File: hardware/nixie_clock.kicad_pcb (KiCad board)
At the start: 2 copper layers, 224 x 70 mm, 66 parts, among them J1 Conn_02x02_Odd_Even, J2 USB_C_Receptacle_USB2.0_16P, J3 Conn_01x04, Q1 IRF740, SW1 SW_SPST, SW2 SW_SPST, U1 AP63203WU, U2 MAX1771xSA, U3 ESP32-C3-WROOM-02, U4 HV5622PG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

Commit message: Change power connector.
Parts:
- J3: value Conn_01x04 -> Conn_01x03; footprint TerminalBlock_Phoenix:TerminalBlock_Phoenix_PT-1,5-4-3.5-H_1x04_P3.50mm_Horizontal -> TerminalBlock_Phoenix:TerminalBlock_Phoenix_PT-1,5-3-3.5-H_1x03_P3.50mm_Horizontal
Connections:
- J3 pad 3: /connectors/GND -> /connectors/12V
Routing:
- net /connectors/12V: track 326.0 -> 330.2 mm
- net /connectors/GND: track 118.5 -> 117.7 mm

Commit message: Rework some tracks.
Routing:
- net Net-(J1-Pin_3): track 11.7 -> 13.5 mm
- net /cpu/GPIO1: track 155.9 -> 157.5 mm
- net /cpu/GPIO2: track 154.1 -> 155.3 mm
- net /driver_3_digits_1_dot_left/SPI_SDO: track 147.0 -> 148.0 mm
- net /connectors/GND: track 117.7 -> 118.6 mm
- net Net-(J1-Pin_1): track 11.0 -> 11.8 mm

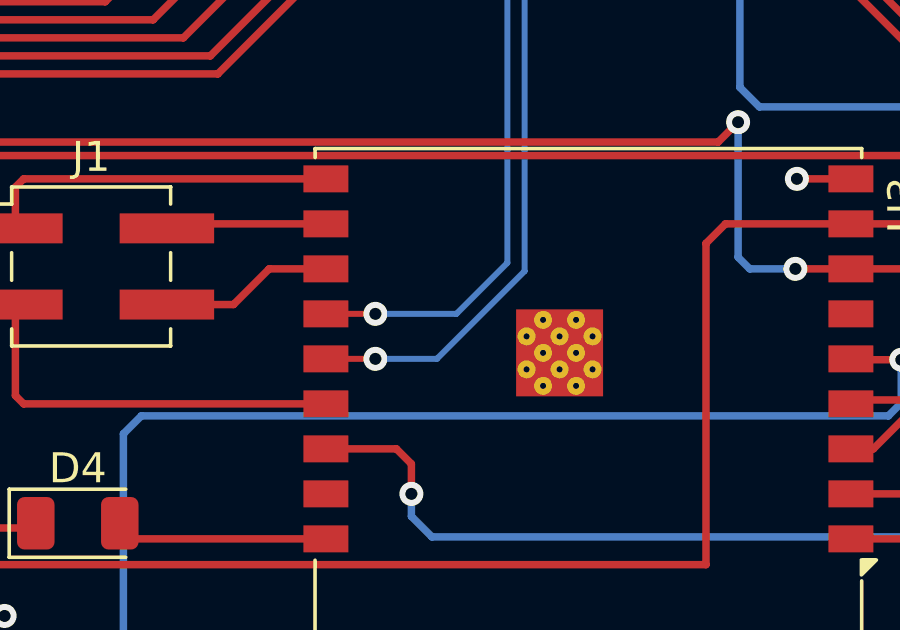
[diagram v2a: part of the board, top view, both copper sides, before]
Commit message: Fix USB lane size.
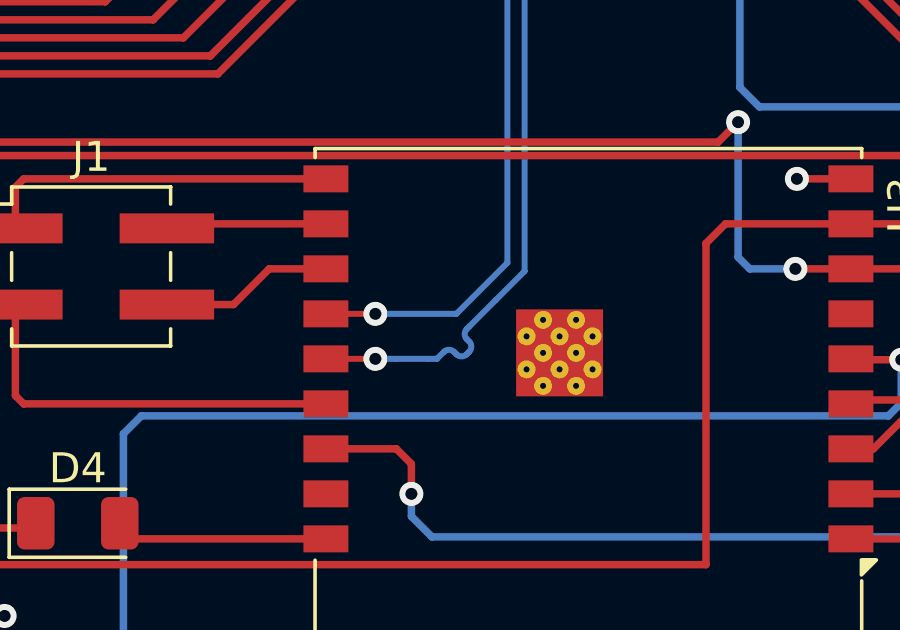
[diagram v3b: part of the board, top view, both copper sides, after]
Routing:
- net /connectors/D+: track 56.4 -> 57.1 mm
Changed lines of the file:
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@@
 	)
 	(segment
+		(start 157.641741 115.646581)
+		(end 157.726593 115.561728)
+		(width 0.2)
+		(layer "B.Cu")
+		(net 24)
+	)
+	(segment
 		(start 154.6 115.8)
+		(end 155.279866 115.8)
+		(width 0.2)
+		(layer "B.Cu")
+		(net 24)
+	)
+	(segment
+		(start 155.279866 115.8)
+		(end 156.351108 115.8)
+		(width 0.2)
+		(layer "B.Cu")
+		(net 24)
+	)
+	(segment
+		(start 156.65 115.8)
+		(end 156.883169 115.566831)
+		(width 0.2)
+		(layer "B.Cu")
+		(net 24)
+	)
+	(segment
+		(start 158.608049 113.841951)
+		(end 159.574 112.876)
+		(width 0.2)
+		(layer "B.Cu")
+		(net 24)
+	)
+	(segment
+		(start 159.574 73.601)
+		(end 161.075 72.1)
+		(width 0.2)
+		(layer "B.Cu")
+		(net 24)
+	)
+	(segment
+		(start 156.351108 115.8)
 		(end 156.65 115.8)
 		(width 0.2)
@@
 	)
 	(segment
+		(start 157.731697 114.718302)
+		(end 158.608049 113.841951)
+		(width 0.2)
+		(layer "B.Cu")
+		(net 24)
+	)
+	(segment
+		(start 157.646842 114.803154)
+		(end 157.731697 114.718302)
+		(width 0.2)
+		(layer "B.Cu")
+		(net 24)
+	)
+	(segment
+		(start 157.726593 115.222316)
+		(end 157.646842 115.142565)
+		(width 0.2)
+		(layer "B.Cu")
+		(net 24)
+	)
+	(segment
 		(start 161.075 72.1)
 		(end 162.505 72.1)
@@
 	)
 	(segment
-		(start 159.574 73.601)
-		(end 161.075 72.1)
+		(start 157.22258 115.566831)
+		(end 157.30233 115.646581)
 		(width 0.2)
 		(layer "B.Cu")
 		(net 24)
 	)
-	(segment
-		(start 156.65 115.8)
-		(end 159.574 112.876)
+	(arc
+		(start 156.883169 115.566831)
+		(mid 157.052874 115.496537)
+		(end 157.22258 115.566831)
+		(width 0.2)
+		(layer "B.Cu")
+		(net 24)
+	)
+	(arc
+		(start 157.30233 115.646581)
+		(mid 157.472036 115.716875)
+		(end 157.641741 115.646581)
+		(width 0.2)
+		(layer "B.Cu")
+		(net 24)
+	)
+	(arc
+		(start 157.726593 115.561728)
+		(mid 157.796888 115.392022)
+		(end 157.726593 115.222316)
+		(width 0.2)
+		(layer "B.Cu")
+		(net 24)
+	)
+	(arc
+		(start 157.646842 115.142565)
+		(mid 157.576547 114.97286)
+		(end 157.646842 114.803154)
 		(width 0.2)
 		(layer "B.Cu")
@@
 		)
 	)
+	(generated
+		(type tuning_pattern)
+		(name "Tuning Pattern")
+		(layer "B.Cu")
+		(base_line
+			(pts
+				(xy 155.279866 115.8) (xy 156.351108 115.8)
+			)
+		)
+		(corner_radius_percent 80)
+		(end
+			(xy 156.351108 115.8)
+		)
+		(initial_side "right")
+		(last_diff_pair_gap 0.18)
+		(last_netname "/connectors/D+")
+		(last_status "too_short")
+		(last_track_width 0.2)
+		(last_tuning "57,0357 mm (trop court)")
+		(max_amplitude 1)
+		(min_amplitude 0.2)
+		(min_spacing 0.6)
+		(origin
+			(xy 155.279866 115.8)
+		)
+		(override_custom_rules no)
+		(rounded yes)
+		(single_sided no)
+		(target_length 57.8092)
+		(target_length_max 57.9092)
+		(target_length_min 57.7092)
+		(target_skew 0)
+		(target_skew_max 0.1)
+		(target_skew_min -0.1)
+		(tuning_mode "single")
+		(members "35a16607-4558-4146-b2c9-206f343f8f7a")
+	)
+	(generated
+		(type tuning_pattern)
+		(name "Tuning Pattern")
+		(layer "B.Cu")
+		(base_line
+			(pts
+				(xy 156.883169 115.566831) (xy 158.608049 113.841951)
+			)
+		)
+		(corner_radius_percent 80)
+		(end
+			(xy 158.608049 113.841951)
+		)
+		(initial_side "right")
+		(last_diff_pair_gap 0.18)
+		(last_netname "/connectors/D+")
+		(last_status "tuned")
+		(last_track_width 0.2)
+		(last_tuning "57,8092 mm (ajusté)")
+		(max_amplitude 1)
+		(min_amplitude 0.2)
+		(min_spacing 0.6)
+		(origin
+			(xy 156.883169 115.566831)
+		)
+		(override_custom_rules no)
+		(rounded yes)
+		(single_sided no)
+		(target_length 57.8092)
+		(target_length_max 57.9092)
+		(target_length_min 57.7092)
+		(target_skew 0)
+		(target_skew_max 0.1)
+		(target_skew_min -0.1)
+		(tuning_mode "single")
+		(members "10d51b2e-0cfd-4ea9-9fbd-f867cd2565ff" "2f0039b8-3d12-499b-b6d5-722cef66da14"
+			"43471335-dcd3-473c-9966-2fbfc5f6b28a" "827e569f-865e-4788-9102-c9e4cfe451c1"
+			"8304e2b3-48c7-4640-b10f-659ee7d3a333" "ae3a55cf-1371-4bb7-a879-6f522ee4415f"
+			"b6cabc14-bdd9-48b6-9e6e-1bb628890a75" "d4c22933-05fe-4d9c-92d0-15b38f3d8719"
+			"e83793f2-18ec-4369-a5a5-8c4f12520b5f"
+		)
+	)

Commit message: Fix DRC errors.
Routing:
- net /connectors/12V: track 330.2 -> 326.8 mm
- net Net-(N4-PadA): track 0.07 -> 2.09 mm
- net /connectors/GND: track 118.6 -> 118.1 mm
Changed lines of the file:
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@@
 		(tags "capacitor")
 		(property "Reference" "C3"
-			(at 0 -1.68 270)
+			(at -2.675 0 270)
 			(layer "F.SilkS")
 			(effects
@@
 		(tags "D2PAK DDPAK TO-263 D2PAK-3 TO-263-3 SOT-404")
 		(property "Reference" "Q1"
-			(at 0 -6.65 90)
+			(at -7.6 0.025 90)
 			(layer "F.SilkS")
 			(effects
@@
 		(tags "capacitor")
 		(property "Reference" "C4"
-			(at 0 -1.68 0)
+			(at 2.8 0 0)
 			(layer "F.SilkS")
 			(effects
@@
 		)
 		(property "Value" "100nF"
-			(at 0 1.68 0)
+			(at 0 -1.6 0)
 			(layer "F.Fab")
 			(effects
@@
 		(tags "mountinghole M3")
 		(property "Reference" "H4"
-			(at 0 -4.15 0)
+			(at 0 -4.5 0)
 			(layer "F.SilkS")
 			(effects
@@
 		(tags "mountinghole M3")
 		(property "Reference" "H1"
-			(at 0 -4.15 0)
+			(at 0 4.5 0)
 			(layer "F.SilkS")
 			(effects
@@
 		(tags "mountinghole M3")
 		(property "Reference" "H3"
-			(at 0 -4.15 0)
+			(at 0 -4.5 0)
 			(layer "F.SilkS")
 			(effects
@@
 		(tags "capacitor")
 		(property "Reference" "C2"
-			(at 0 -1.68 0)
+			(at 2.8 -0.035 0)
 			(layer "F.SilkS")
 			(effects
@@
 		(tags "resistor")
 		(property "Reference" "R21"
-			(at 0 -1.83 0)
+			(at 3.8 0 0)
 			(layer "F.SilkS")
 			(effects
@@
 		)
 		(property "Value" "10k"
-			(at 0 1.83 0)
+			(at -0.01 -1.75 0)
 			(layer "F.Fab")
 			(effects
@@
 		(tags "resistor")
 		(property "Reference" "R22"
-			(at 0 -1.83 0)
+			(at 3.8 0 0)
 			(layer "F.SilkS")
 			(effects
@@
 		(tags "mountinghole M3")
 		(property "Reference" "H2"
-			(at 0 -4.15 0)
+			(at 0 4.5 0)
 			(layer "F.SilkS")
 			(effects
@@
 	)
 	(segment
+		(start 140.25 62)
+		(end 140 62.25)
+		(width 0.25)
+		(layer "B.Cu")
+		(net 13)
+	)
+	(segment
 		(start 178.55 80)
 		(end 208.75 80)
@@
 	)
 	(segment
+		(start 140 62.25)
+		(end 140 66.475)
+		(width 0.25)
+		(layer "B.Cu")
+		(net 13)
+	)
+	(segment
 		(start 178 79.45)
 		(end 178.55 80)
@@
 	)
 	(segment
-		(start 136.56 66.5)
-		(end 136.5 66.5)
-		(width 0.25)
-		(layer "B.Cu")
-		(net 13)
-	)
-	(segment
 		(start 178 62.6)
 		(end 177.4 62)
@@
 	)
 	(segment
-		(start 136.5 62.75)
-		(end 136.5 66.5)
-		(width 0.25)
-		(layer "B.Cu")
-		(net 13)
-	)
-	(segment
-		(start 137.25 62)
-		(end 136.5 62.75)
+		(start 177.4 62)
+		(end 140.25 62)
 		(width 0.25)
 		(layer "B.Cu")
@@
 	)
 	(segment
-		(start 177.4 62)
-		(end 137.25 62)
-		(width 0.25)
-		(layer "B.Cu")
-		(net 13)
-	)
-	(segment
-		(start 136.5 66.44)
-		(end 136.56 66.5)
-		(width 0.25)
-		(layer "B.Cu")
-		(net 13)
-	)
-	(segment
 		(start 178 78)
 		(end 178 62.6)
@@
 	)
 	(segment
+		(start 167.85 72.075)
+		(end 167.975416 72.200416)
+		(width 0.25)
+		(layer "F.Cu")
+		(net 32)
+	)
+	(segment
 		(start 142.2325 124.3625)
 		(end 142.24 124.37)
@@
 	)
 	(segment
-		(start 169.005 72)
-		(end 169.005 72.200416)
-		(width 0.25)
-		(layer "F.Cu")
-		(net 32)
-	)
-	(segment
 		(start 172.0375 76.173197)
 		(end 171.326803 76.173197)
@@
 	)
 	(segment
-		(start 160 68.84)
-		(end 160 69.5)
-		(width 0.25)
-		(layer "F.Cu")
-		(net 32)
-	)
-	(segment
-		(start 166.4 69.395)
-		(end 169.005 72)
-		(width 0.25)
-		(layer "F.Cu")
-		(net 32)
-	)
-	(segment
 		(start 224.2 121.125)
 		(end 224.2 122.8)
@@
 	)
 	(segment
-		(start 99.775 122.995)
-		(end 99.78 123)
-		(width 0.25)
-		(layer "F.Cu")
-		(net 32)
-	)
-	(segment
 		(start 225.8 121.125)
 		(end 225.8 122.45)
@@
 	)
 	(segment
-		(start 98.3 119.625)
+		(start 99 119.625)
 		(end 99.65 119.625)
 		(width 0.25)
@@
 	)
 	(segment
+		(start 98.3 119.625)
+		(end 99 119.625)
+		(width 0.25)
+		(layer "F.Cu")
+		(net 32)
+	)
+	(segment
 		(start 213.04 86.805)
 		(end 213.04 88.69)
@@
 	)
 	(segment
-		(start 99.775 121.125)
-		(end 99.775 122.995)
-		(width 0.25)
-		(layer "F.Cu")
-		(net 32)
-	)
-	(segment
 		(start 68.805 69.545)
 		(end 68.805 70.285)
@@
 	)
 	(segment
+		(start 166.575 70.975)
+		(end 167.85 70.975)
+		(width 0.25)
+		(layer "F.Cu")
+		(net 32)
+	)
+	(segment
 		(start 159.99 71.01)
 		(end 159 72)
@@
 	)
 	(segment
+		(start 166.4 70.8)
+		(end 166.575 70.975)
+		(width 0.25)
+		(layer "F.Cu")
+		(net 32)
+	)
+	(segment
 		(start 105.25 125.5)
 		(end 105.22 125.53)
@@
 	)
 	(segment
+		(start 99 119.625)
+		(end 99 119)
+		(width 0.25)
+		(layer "F.Cu")
+		(net 32)
+	)
+	(segment
 		(start 140.5 124.3625)
 		(end 142.2325 124.3625)
@@
 	)
 	(segment
+		(start 166.4 69.395)
+		(end 166.4 70.8)
+		(width 0.25)
+		(layer "F.Cu")
+		(net 32)
+	)
+	(segment
 		(start 114.565 72.285)
 		(end 114.565 73.34)
@@
 	)
 	(segment
+		(start 167.85 70.975)
+		(end 167.85 72.075)
+		(width 0.25)
+		(layer "F.Cu")
+		(net 32)
+	)
+	(segment
 		(start 193.275 77.775)
 		(end 193.275 75.95)
@@
 	)
 	(segment
+		(start 167.975416 72.200416)
+		(end 169.005 72.200416)
+		(width 0.25)
+		(layer "F.Cu")
+		(net 32)
+	)
+	(segment
 		(start 129.58 73.165)
 		(end 127.555 73.165)
@@
 	)
 	(via
-		(at 170.5 70.5)
+		(at 99 119)
 		(size 0.8)
 		(drill 0.4)
@@
 	)
 	(via
-		(at 142.24 124.37)
+		(at 170.5 70.5)
 		(size 0.8)
 		(drill 0.4)
@@
 	)
 	(via
-		(at 105.25 125.5)
+		(at 142.24 124.37)
 		(size 0.8)
 		(drill 0.4)
@@
 	)
 	(via
-		(at 99.78 123)
+		(at 105.25 125.5)
 		(size 0.8)
 		(drill 0.4)
@@
 		(width 0.25)
 		(layer "F.Cu")
+		(net 90)
+	)
+	(segment
+		(start 146.97 88.78256)
+		(end 147 88.81256)
+		(width 0.25)
+		(layer "F.Cu")
+		(net 90)
+	)
+	(segment
+		(start 146.97 86.8025)
+		(end 146.97 88.78256)
+		(width 0.25)
+		(layer "F.Cu")

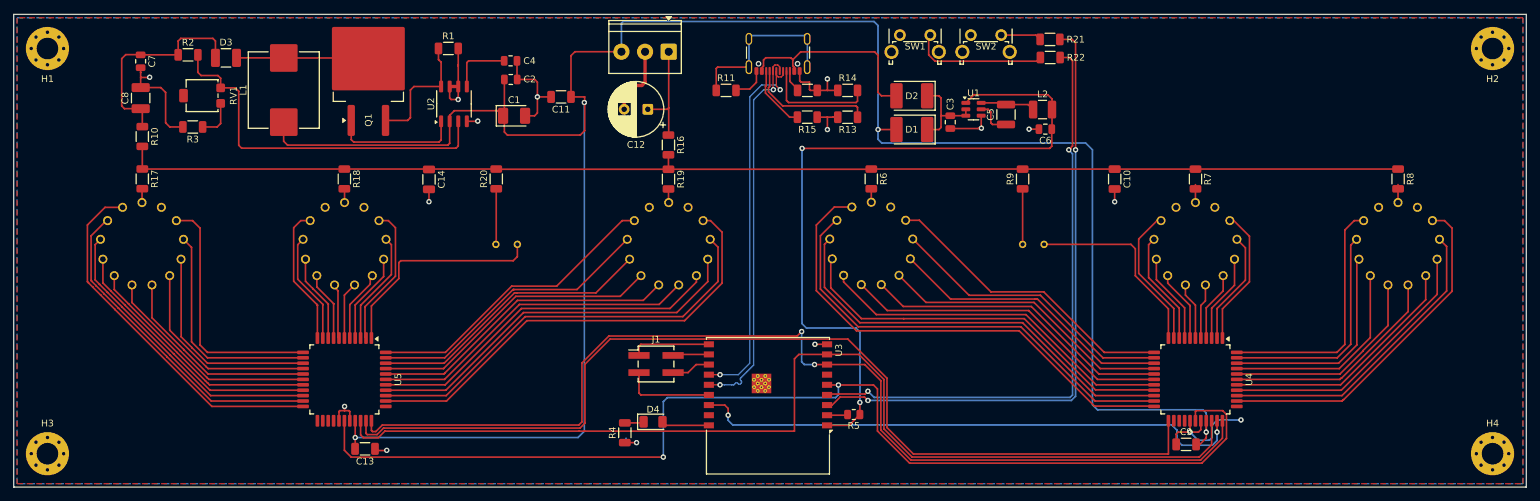
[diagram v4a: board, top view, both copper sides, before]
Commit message: Add clearance of 0.8mm on HV lines for every nixie tube.
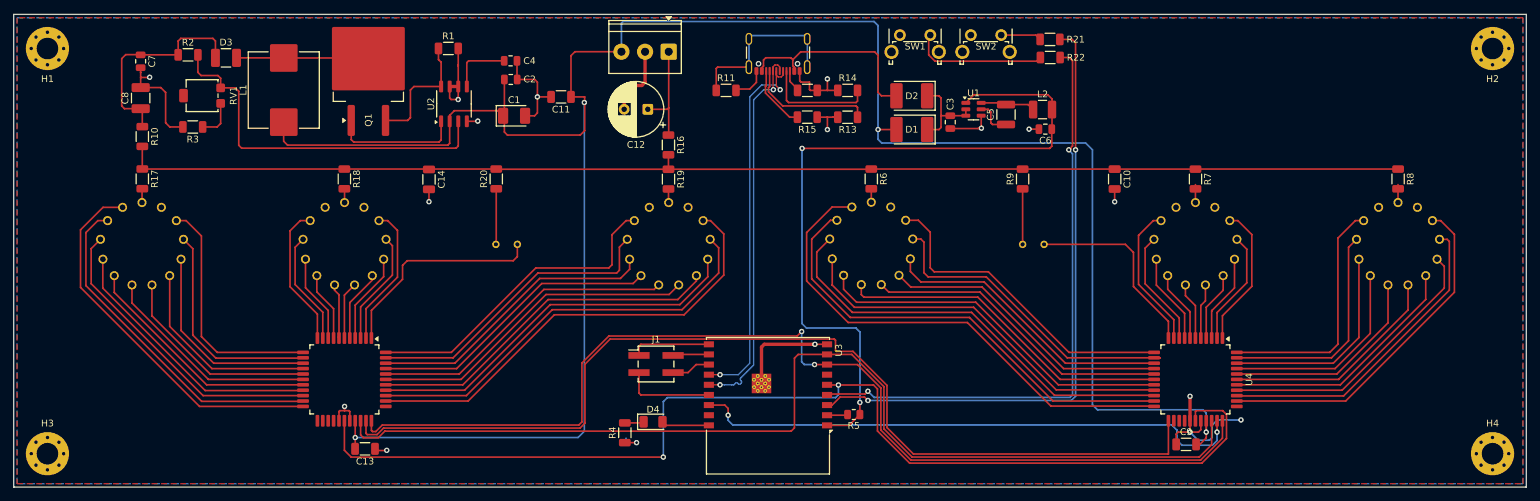
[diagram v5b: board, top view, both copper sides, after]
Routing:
- net /connectors/GND: track 118.1 -> 135.2 mm, vias 16 -> 17
- net Net-(U4D-HVOUT10): track 43.0 -> 46.6 mm
- net Net-(U4D-HVOUT11): track 44.9 -> 48.0 mm
- net Net-(U5B-HVOUT23): track 44.9 -> 47.5 mm
- net Net-(U5D-HVOUT2): track 48.8 -> 51.1 mm
- net Net-(U5D-HVOUT1): track 54.3 -> 56.4 mm
- net Net-(U5B-HVOUT24): track 43.0 -> 45.0 mm
- net Net-(U5D-HVOUT11): track 37.0 -> 35.6 mm
- net Net-(U4D-HVOUT2): track 67.6 -> 69.0 mm
- net Net-(U4D-HVOUT1): track 73.2 -> 74.6 mm
- net Net-(U4B-HVOUT31): track 45.6 -> 46.8 mm
- net Net-(U5D-HVOUT3): track 44.3 -> 45.4 mm
- net Net-(U4D-HVOUT9): track 42.5 -> 43.6 mm
- net Net-(U4B-HVOUT30): track 40.8 -> 41.7 mm
- net Net-(U5B-HVOUT25): track 42.6 -> 43.4 mm
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
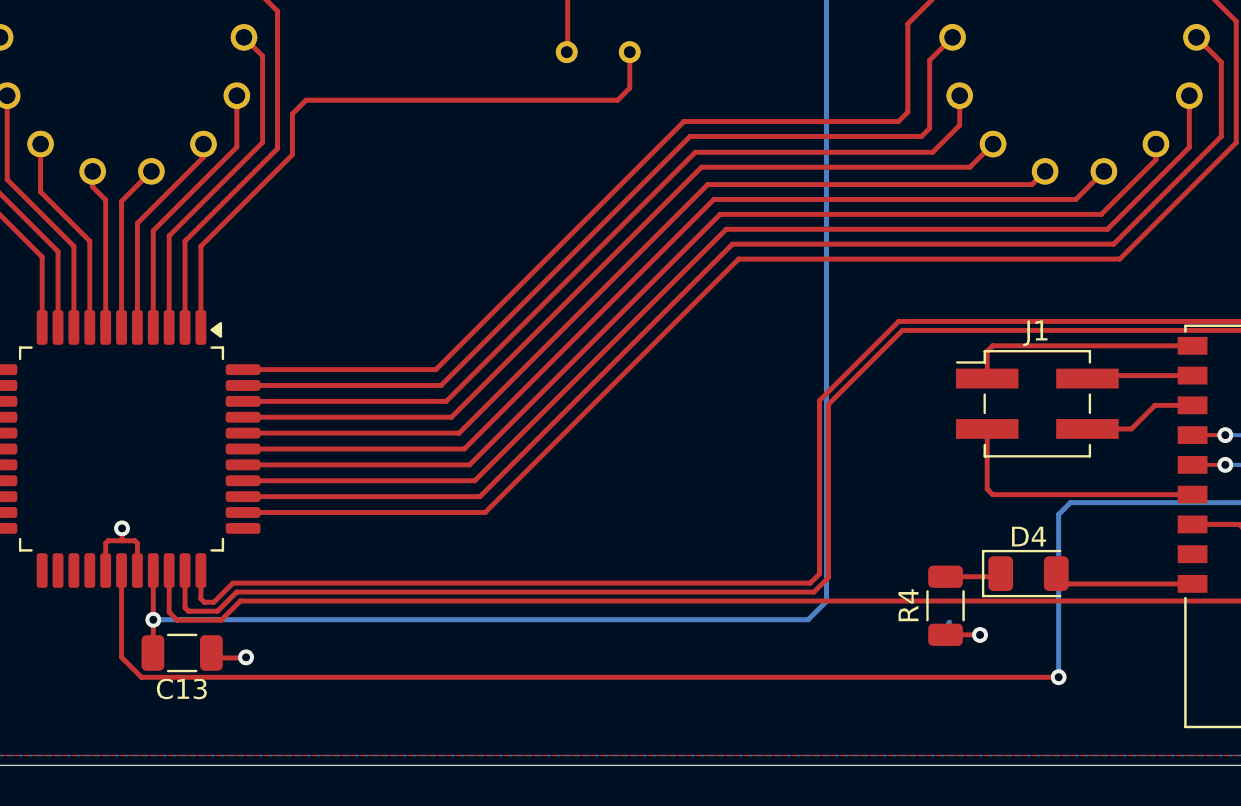
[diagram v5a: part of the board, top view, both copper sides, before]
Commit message: Add space arround C13.
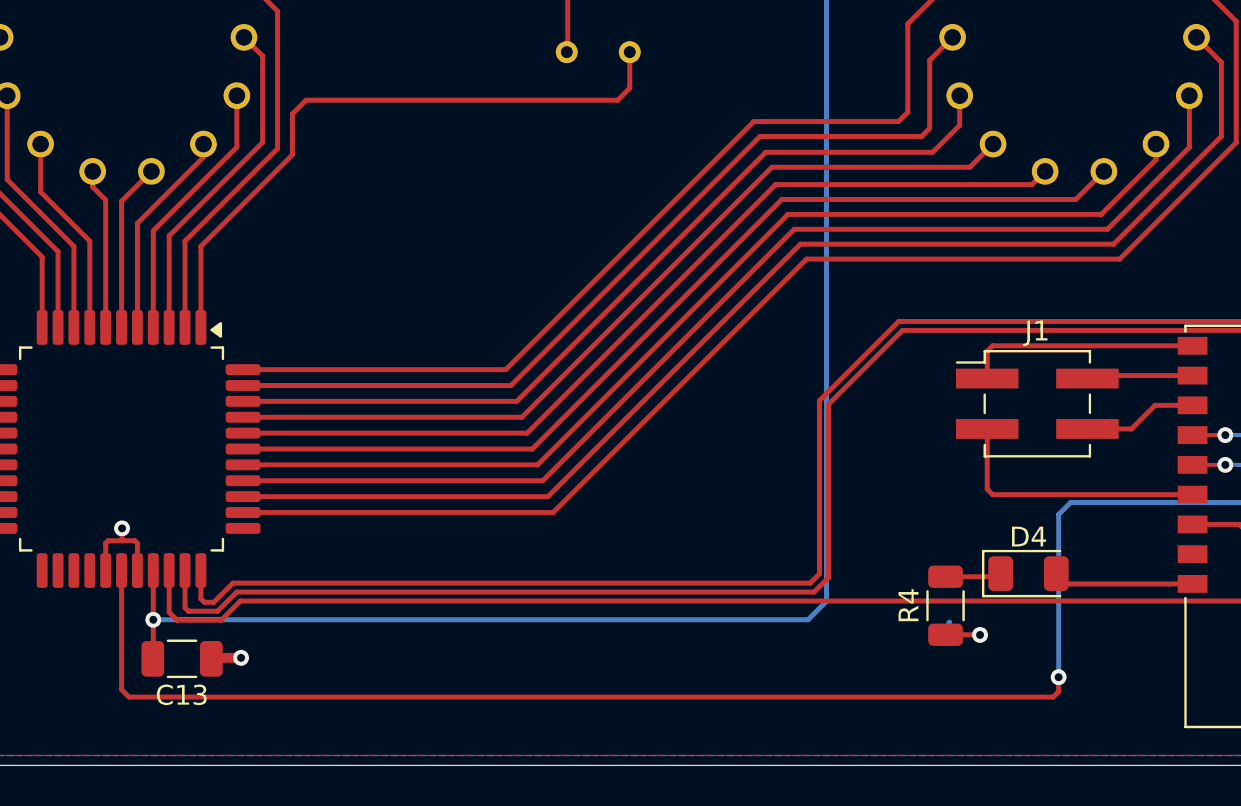
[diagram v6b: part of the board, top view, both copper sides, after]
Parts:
- moved C13 0.30 mm to (102.0, 125.6)
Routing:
- net /cpu/SPI_CLK: track 166.9 -> 169.1 mm
